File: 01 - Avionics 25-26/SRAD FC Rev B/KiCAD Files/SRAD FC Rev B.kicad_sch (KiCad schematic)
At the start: 0 parts

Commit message: Add files via upload
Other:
- added sheet Barometer (Barometer.kicad_sch)
- added sheet GPS (GPS.kicad_sch)
- added sheet High G Accelerometer (High G Accelerometer.kicad_sch)
- added sheet IMU (IMU.kicad_sch)
- added sheet Microcontroller (Microcontroller.kicad_sch)
- added sheet Power (Power.kicad_sch)
- added sheet Pyro (Pyro.kicad_sch)
- added sheet RF Module (RF Module.kicad_sch)
- added sheet Storage (Storage.kicad_sch)

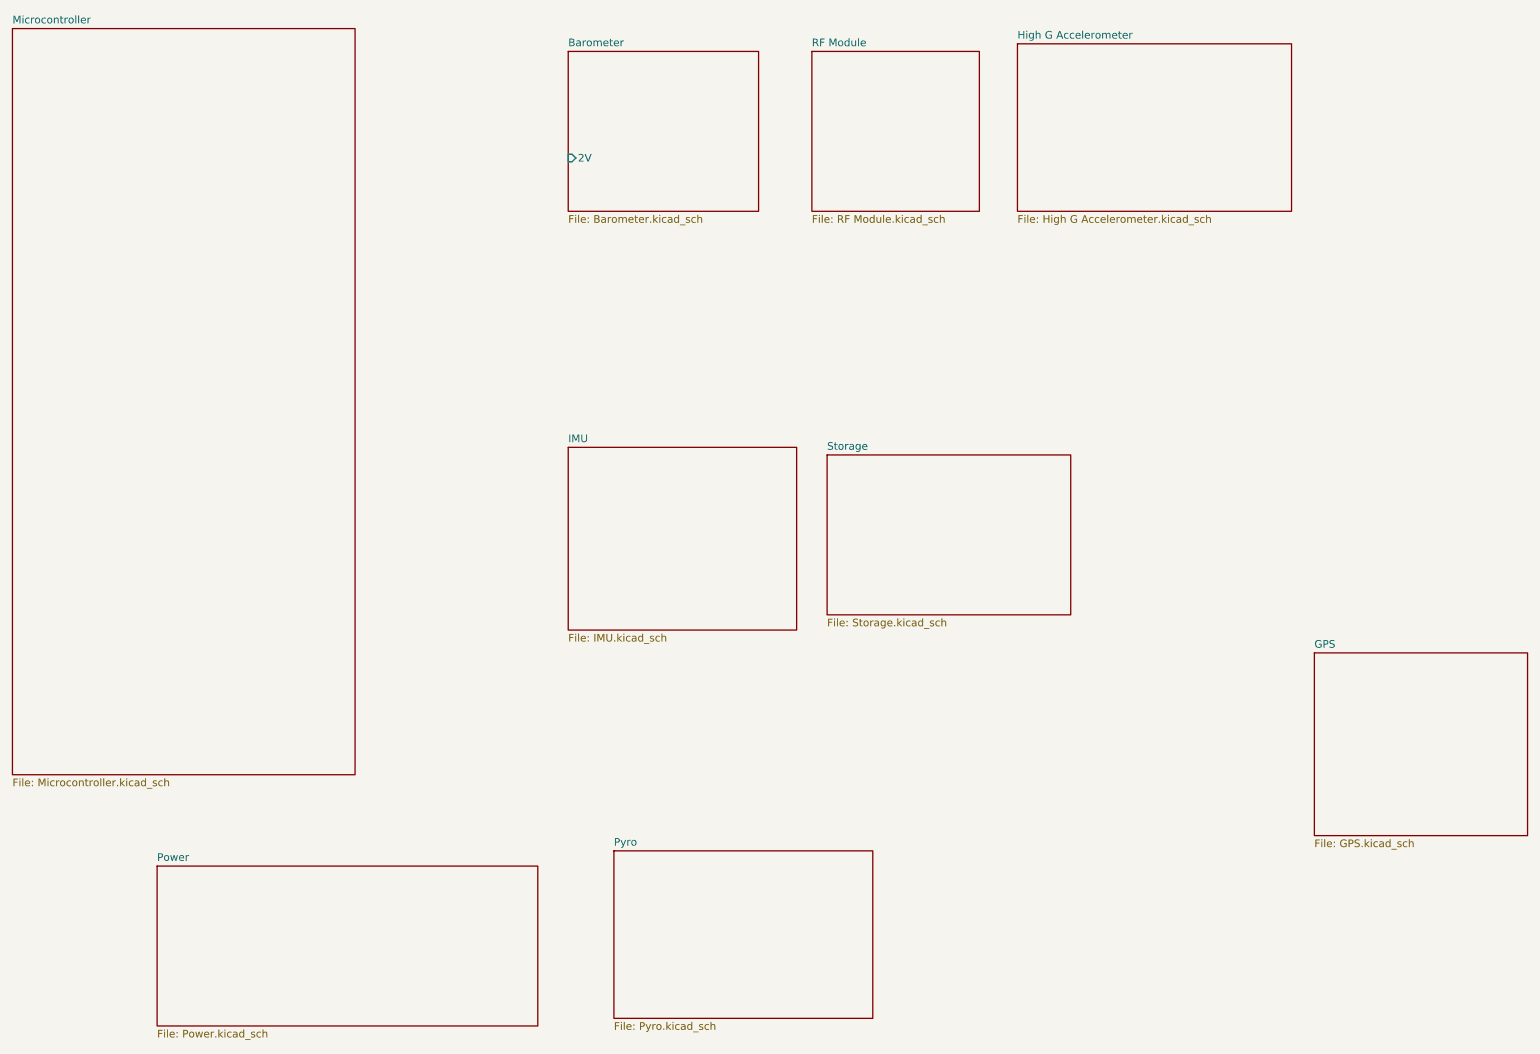
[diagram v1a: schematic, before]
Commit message: adjusted the root page
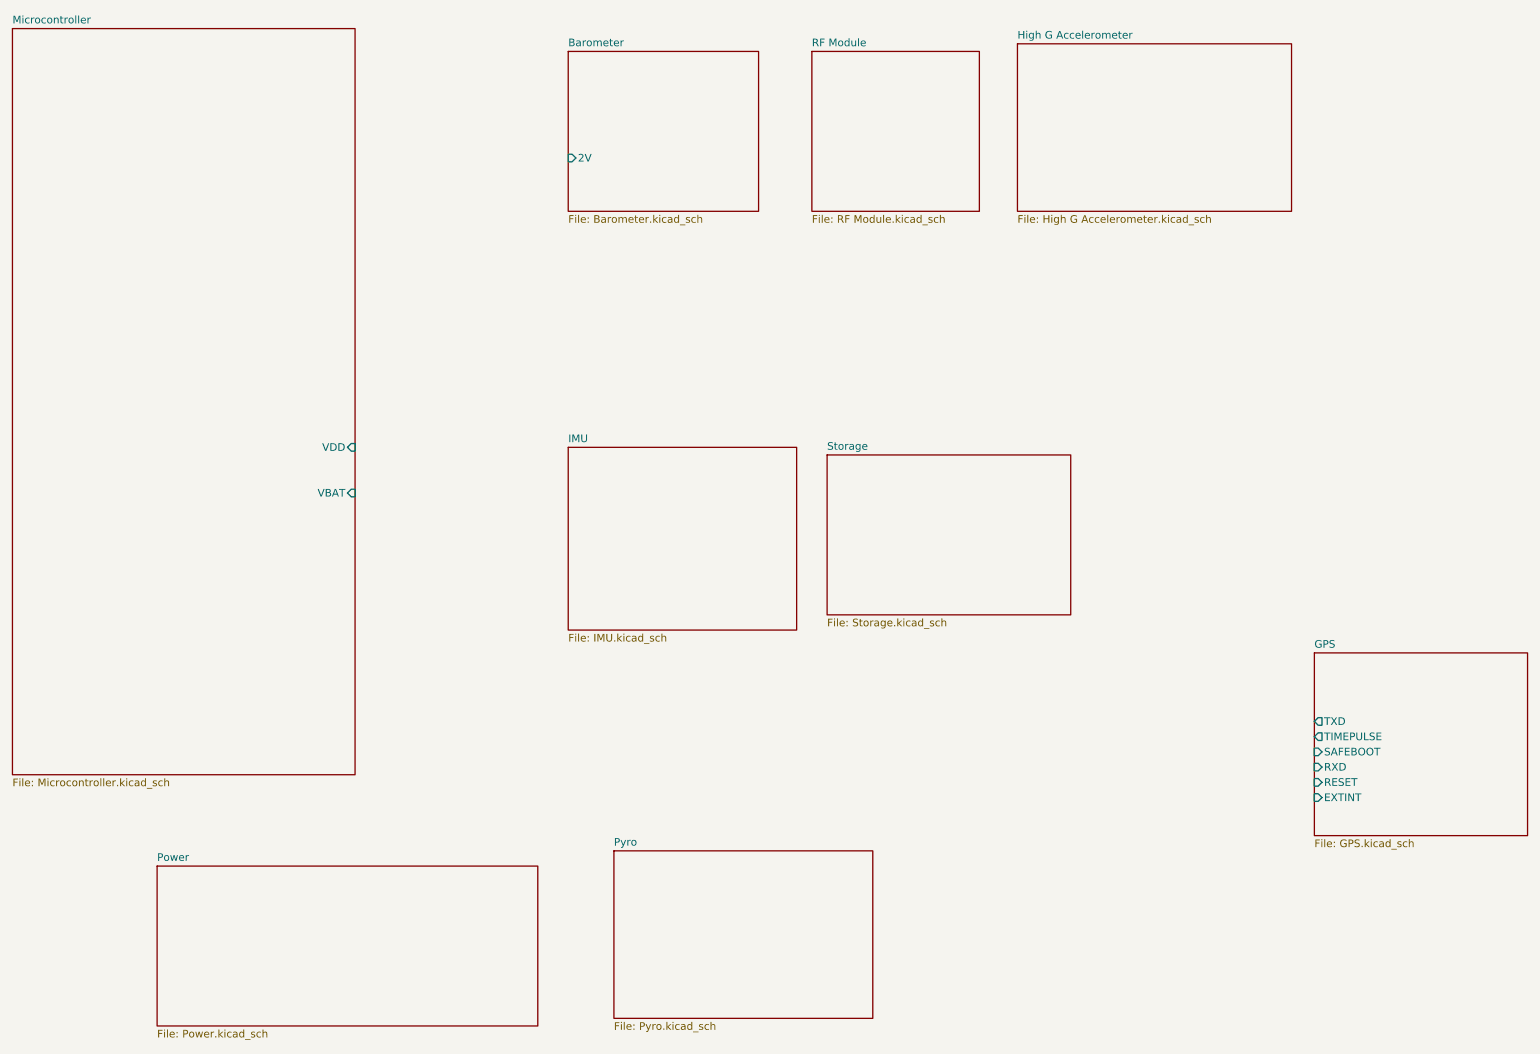
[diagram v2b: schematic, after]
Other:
- sheet GPS ports: added EXTINT, RESET, RXD, SAFEBOOT, TIMEPULSE, TXD; removed none
- sheet Microcontroller ports: added VBAT, VDD; removed none
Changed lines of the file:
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@@
+			)
+		)
+		(pin "VBAT" input
+			(at 78.74 100.33 0)
+			(effects
+				(font
+					(size 1.27 1.27)
+				)
+				(justify right)
+			)
+		)
+		(pin "VDD" input
+			(at 78.74 92.71 0)
+			(effects
+				(font
+					(size 1.27 1.27)
+				)
+				(justify right)
 			)
 		)
@@
 			)
 		)
+		(pin "EXTINT" input
+			(at 238.76 151.13 180)
+			(effects
+				(font
+					(size 1.27 1.27)
+				)
+				(justify left)
+			)
+		)
+		(pin "RESET" input
+			(at 238.76 148.59 180)
+			(effects
+				(font
+					(size 1.27 1.27)
+				)
+				(justify left)
+			)
+		)
+		(pin "RXD" input
+			(at 238.76 146.05 180)
+			(effects
+				(font
+					(size 1.27 1.27)
+				)
+				(justify left)
+			)
+		)
+		(pin "SAFEBOOT" input
+			(at 238.76 143.51 180)
+			(effects
+				(font
+					(size 1.27 1.27)
+				)
+				(justify left)
+			)
+		)
+		(pin "TIMEPULSE" output
+			(at 238.76 140.97 180)
+			(effects
+				(font
+					(size 1.27 1.27)
+				)
+				(justify left)
+			)
+		)
+		(pin "TXD" output
+			(at 238.76 138.43 180)
+			(effects
+				(font
+					(size 1.27 1.27)
+				)
+				(justify left)
+			)
+		)

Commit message: Adjusted the readme to add the manager and adjusted the sheet authors, date, name, and company
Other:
- company: (none) -> Missouri S&T Rocket Design Team
- title: (none) -> SRAD FC Revision B
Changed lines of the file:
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@@
 	(generator_version "9.0")
 	(paper "A4")
+	(title_block
+		(title "SRAD FC Revision B")
+		(date "2025-11-01")
+		(rev "B")
+		(company "Missouri S&T Rocket Design Team")
+		(comment 1 "Author(s): Aaron Brinker, Isaac Lough, Joseph Hinchie, Ryan Newey, and Ian Butrick")
+	)
 	(sheet
 		(at 45.72 162.56)

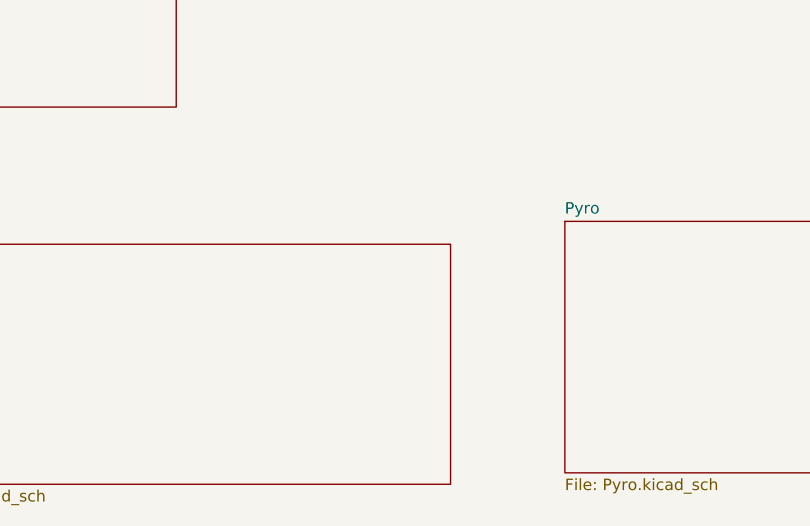
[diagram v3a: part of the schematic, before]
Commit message: made part of the power circuit for the microcontroller
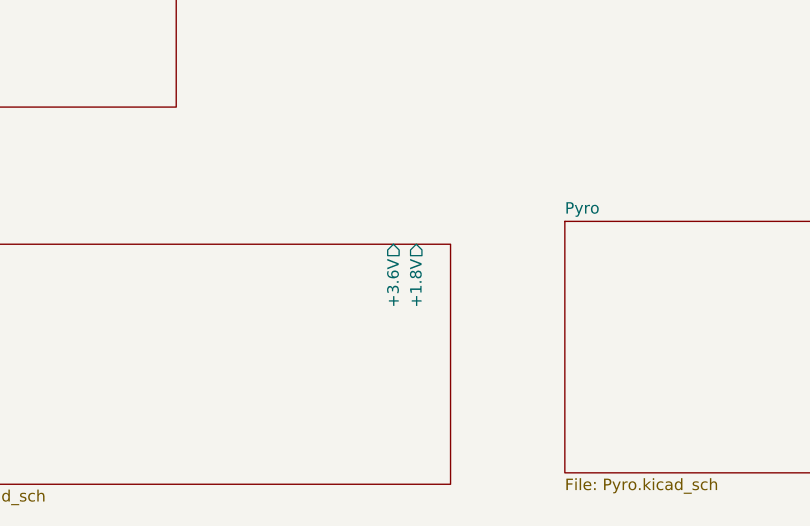
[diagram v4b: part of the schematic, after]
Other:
- sheet Power ports: added +1.8V, +3.6V; removed none
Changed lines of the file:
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@@
+			)
+		)
+		(pin "+3.6V" output
+			(at 102.87 162.56 90)
+			(effects
+				(font
+					(size 1.27 1.27)
+				)
+				(justify right)
+			)
+		)
+		(pin "+1.8V" output
+			(at 105.41 162.56 90)
+			(effects
+				(font
+					(size 1.27 1.27)
+				)
+				(justify right)
 			)
 		)
